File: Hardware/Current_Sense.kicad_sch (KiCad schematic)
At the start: 30 parts, among them IC1 INA241A5IDR, IC2 AMC1350DWVR, IC3 OPA396DCKR, J6 Shunt Resistor, J7 Scrut Conn, SW3 Scrut Select, U9 TLV6001DCK

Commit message: op amp
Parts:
- added IC4: TLV9002QDRQ1, SOIC127P600X175-8N, symbol TLV9002QDRQ1:TLV9002QDRQ1
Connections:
- net +3.3V: now also IC4.8 (V+)
- net GND: now also IC4.4 (V-)
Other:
- note added: "TODO: add voltage reference (~ 1.25V)"
- note removed: "TODO: voltage reference (~ 1.25V)"

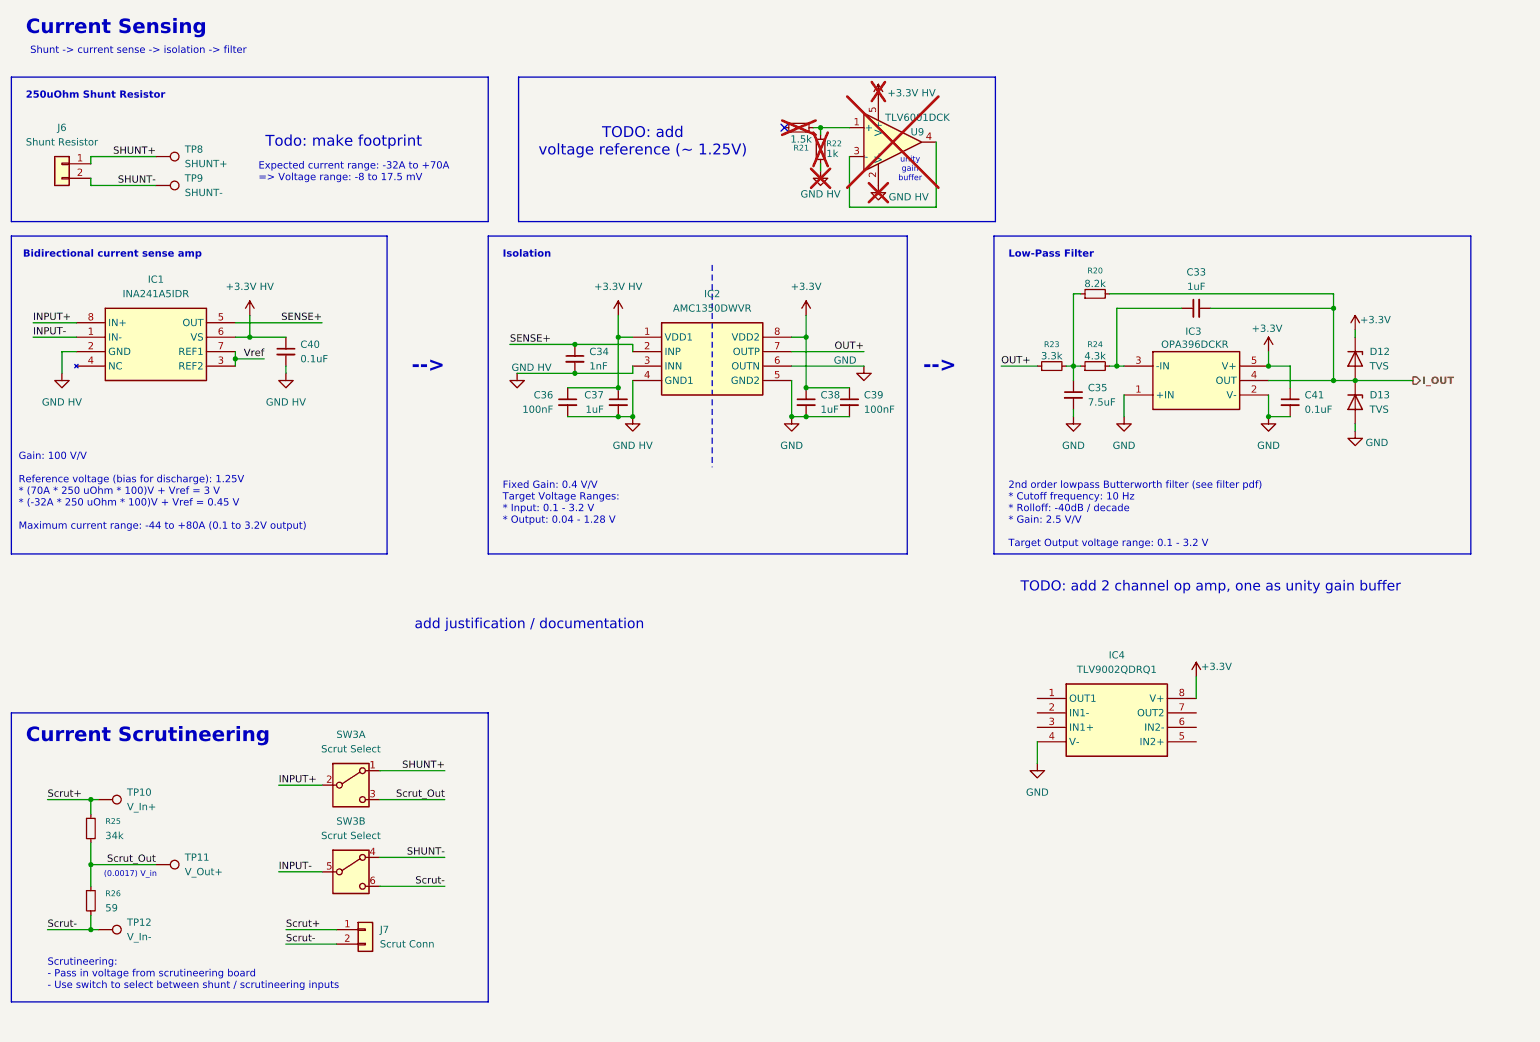
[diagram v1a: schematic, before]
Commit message: changed to 2 channel op amp, stole RPP from PSOM
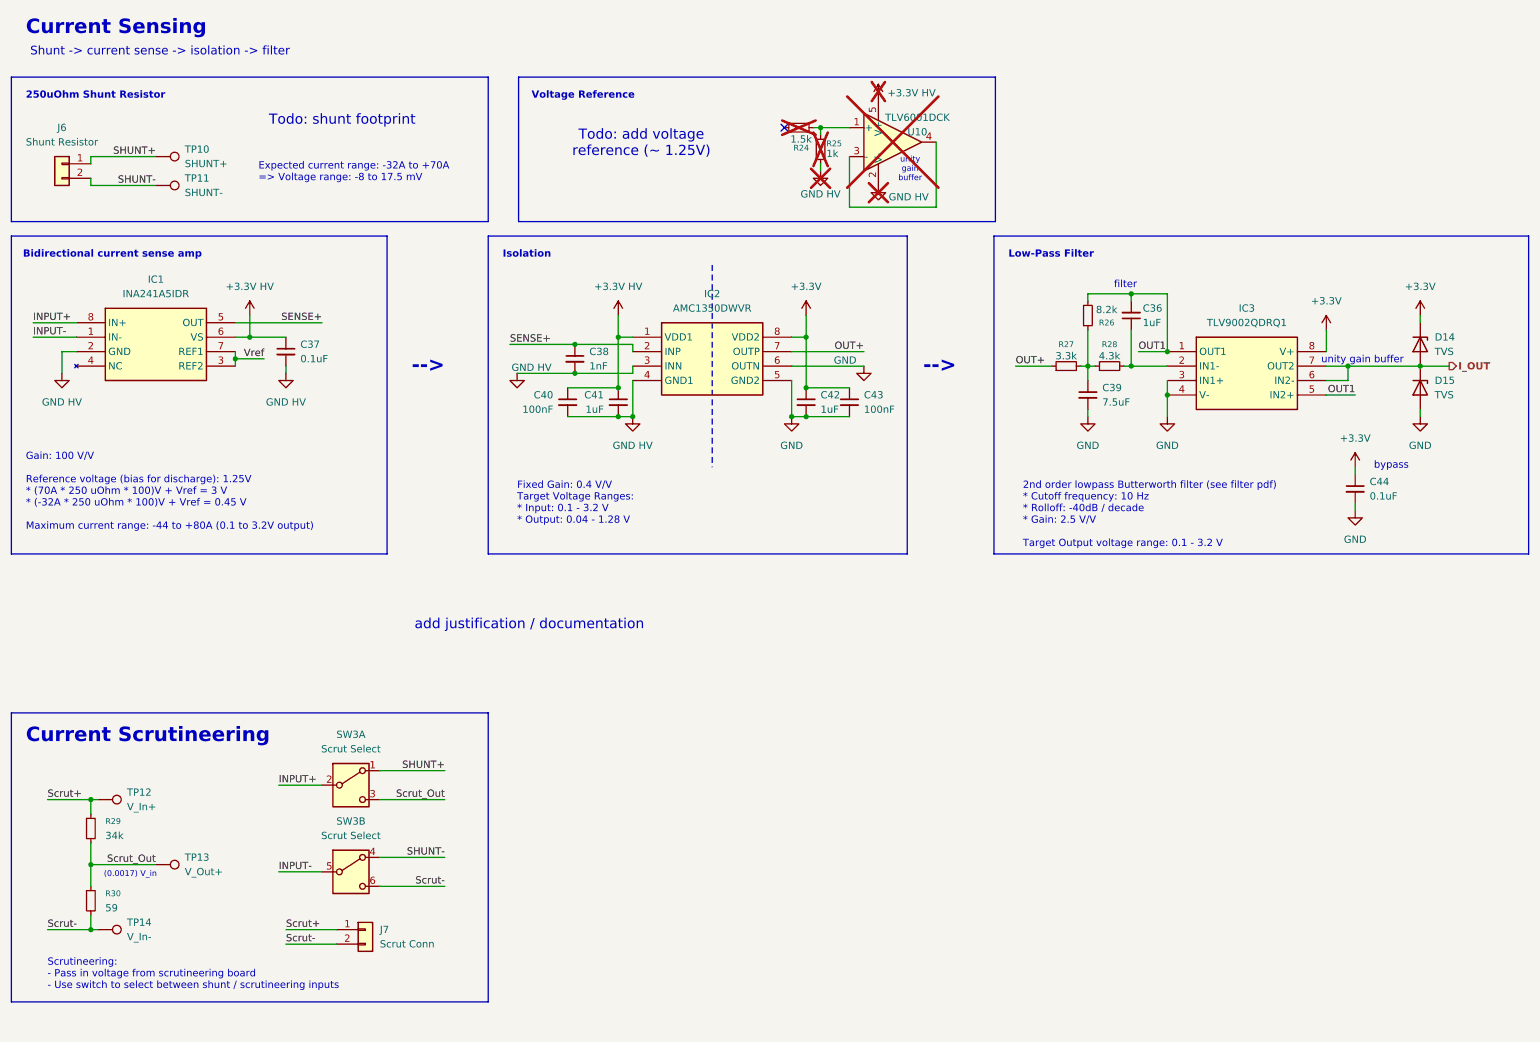
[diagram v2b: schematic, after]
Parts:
- removed C33: 1uF, Capacitor_SMD:C_0603_1608Metric_Pad1.08x0.95mm_HandSolder, symbol Device:C_Small
- removed C35: 7.5uF, Capacitor_SMD:C_0603_1608Metric_Pad1.08x0.95mm_HandSolder, symbol Device:C_Small
- removed C41: 0.1uF, Capacitor_SMD:C_0603_1608Metric_Pad1.08x0.95mm_HandSolder, symbol Device:C_Small
- removed D12, D13: TVS, Diode_SMD:D_SOD-123F, symbol Device:D_Zener
- removed IC3: OPA396DCKR, Parts:SOT65P210X110-5N, symbol OPA396DCKR:OPA396DCKR
- removed R20: 8.2k, Resistor_SMD:R_0603_1608Metric_Pad0.98x0.95mm_HandSolder, symbol Device:R_Small
- removed R23: 3.3k, Resistor_SMD:R_0603_1608Metric_Pad0.98x0.95mm_HandSolder, symbol Device:R_Small
- removed R24: 4.3k, Resistor_SMD:R_0603_1608Metric_Pad0.98x0.95mm_HandSolder, symbol Device:R_Small
- added C36: 1uF, Capacitor_SMD:C_0603_1608Metric_Pad1.08x0.95mm_HandSolder, symbol Device:C_Small
- added C39: 7.5uF, Capacitor_SMD:C_0603_1608Metric_Pad1.08x0.95mm_HandSolder, symbol Device:C_Small
- added C44: 0.1uF, Capacitor_SMD:C_0603_1608Metric_Pad1.08x0.95mm_HandSolder, symbol Device:C_Small
- added D14, D15: TVS, Diode_SMD:D_SOD-123F, symbol Device:D_Zener
- added R26: 8.2k, Resistor_SMD:R_0603_1608Metric_Pad0.98x0.95mm_HandSolder, symbol Device:R_Small
- added R27: 3.3k, Resistor_SMD:R_0603_1608Metric_Pad0.98x0.95mm_HandSolder, symbol Device:R_Small
- added R28: 4.3k, Resistor_SMD:R_0603_1608Metric_Pad0.98x0.95mm_HandSolder, symbol Device:R_Small
- renumbered C40 to C37, C34 to C38, C36 to C40, C37 to C41, C38 to C42, C39 to C43, IC4 to IC3, R21 to R24, R22 to R25, R25 to R29, R26 to R30, TP8 to TP10, TP9 to TP11, TP10 to TP12, TP11 to TP13, TP12 to TP14, U9 to U10
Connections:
- net +3.3V: now also C44.1, D14.1 (K)
- net GND: now also IC3.3 (IN1+), C39.2, C44.2, D15.2 (A)
- net I_OUT: now also IC3.6 (IN2-), IC3.7 (OUT2), D14.2 (A), D15.1 (K)
- net OUT+: now also R27.1
- net OUT1: now reaches IC3.1 (OUT1)
- net OUT1: now also IC3.5 (IN2+), C36.2, R26.2
- net at IC3.2 (IN1-): now also C36.1, R28.2
- new net: C39.1, R26.1, R27.2, R28.1
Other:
- note added: "Todo: add voltage reference (~ 1.25V)"
- note added: "Todo: shunt footprint"
- note added: "Voltage Reference"
- note added: "bypass"
- note added: "filter"
- note removed: "TODO: add 2 channel op amp, one as unity gain buffer"
- note removed: "TODO: add voltage reference (~ 1.25V)"
- note removed: "Todo: make footprint"
- moved on the sheet: IC3

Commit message: added voltage reference, shunt model; addressed comments
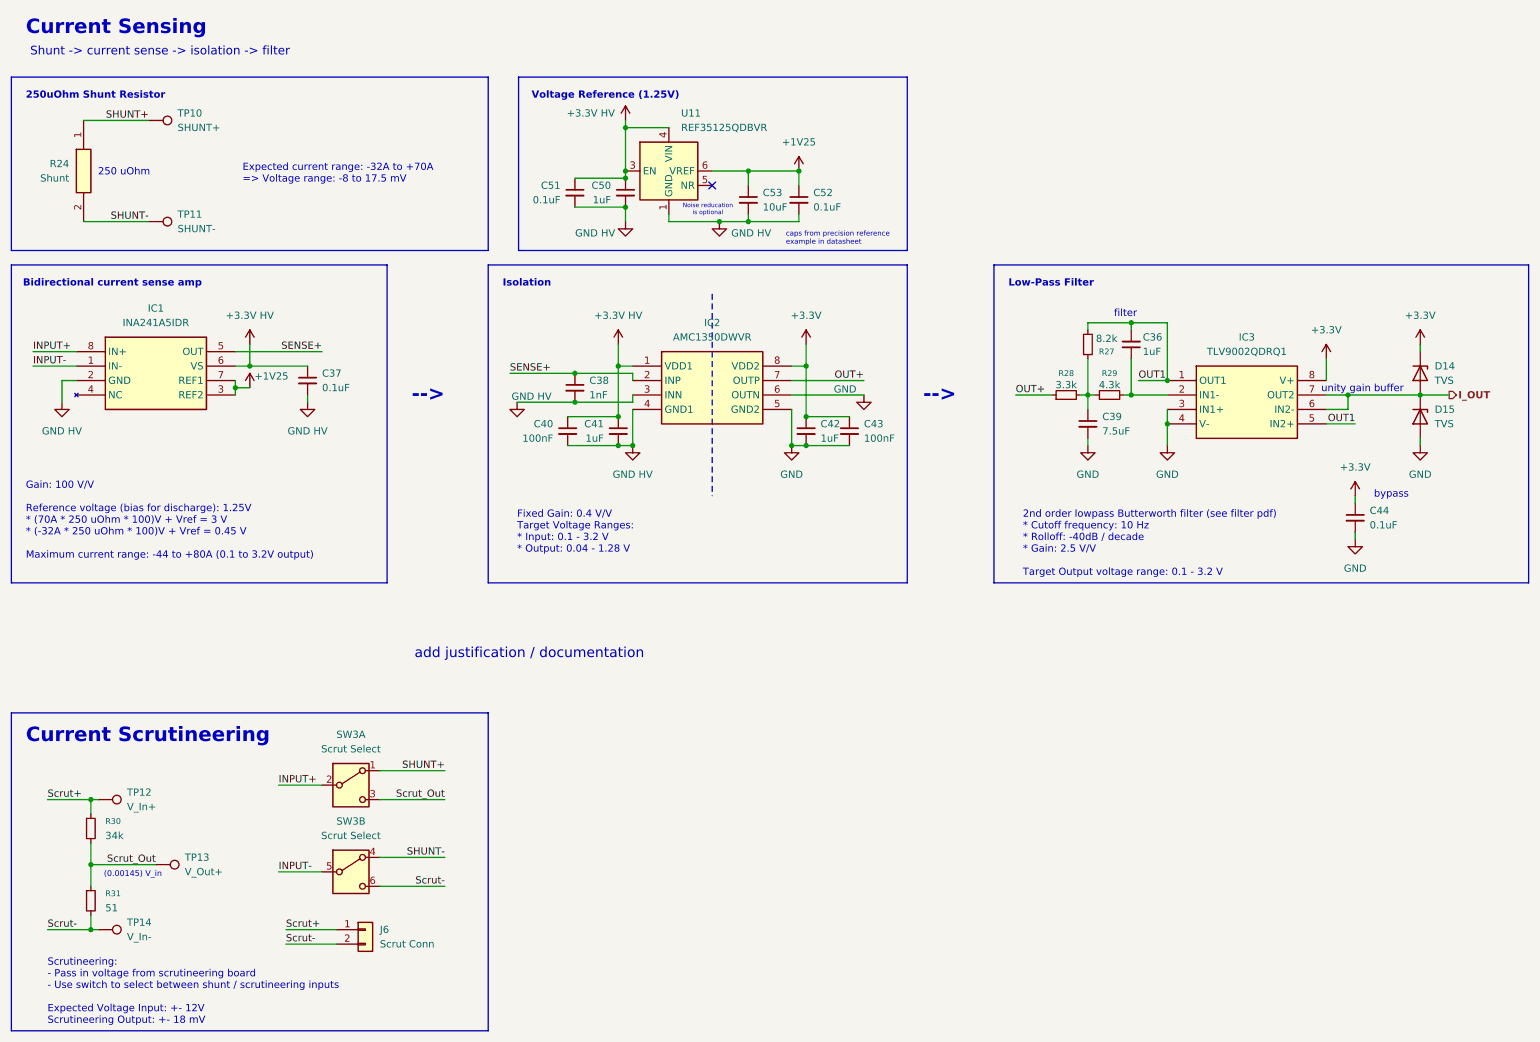
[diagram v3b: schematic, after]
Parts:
- removed J6: Shunt Resistor, symbol Connector_Generic:Conn_01x02
- removed R24: 1.5k, Resistor_SMD:R_0603_1608Metric_Pad0.98x0.95mm_HandSolder, symbol Device:R_Small
- removed R25: 1k, Resistor_SMD:R_0603_1608Metric_Pad0.98x0.95mm_HandSolder, symbol Device:R_Small
- removed U10: TLV6001DCK, Package_TO_SOT_SMD:SOT-353_SC-70-5, symbol Amplifier_Operational:TLV6001DCK
- added C50: 1uF, Capacitor_SMD:C_0603_1608Metric_Pad1.08x0.95mm_HandSolder, symbol Device:C_Small
- added C51, C52: 0.1uF, Capacitor_SMD:C_0603_1608Metric_Pad1.08x0.95mm_HandSolder, symbol Device:C_Small
- added C53: 10uF, Capacitor_SMD:C_0603_1608Metric_Pad1.08x0.95mm_HandSolder, symbol Device:C_Small
- added R24: Shunt, WSBS8518L2500JK, symbol WSBS8518L2500JK:WSBS8518L2500JK
- added U11: REF35125QDBVR, Package_TO_SOT_SMD:SOT-23-6, symbol Reference_Voltage:REF35125QDBVR
- R31: renamed from R30; value 59 -> 51
- renumbered J7 to J6, R26 to R27, R27 to R28, R28 to R29, R29 to R30
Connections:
- net +3.3V HV: now also C50.1, C51.1, U11.3 (EN), U11.4 (VIN)
- net GND HV: now also C50.2, C51.2, C52.2, C53.2, U11.1 (GND), U11.2 (GND)
- net SHUNT+: now also R24.1
- net SHUNT-: now also R24.2
- net Vref renamed +1V25
- net +1V25: now also C52.1, C53.1, U11.6 (VREF)
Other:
- note added: "(0.00145) V_in"
- note added: "250 uOhm"
- note added: "Noise reducation is optional"
- note added: "Scrutineering: - Pass in voltage from scrutineering board - Use switch to select between shunt / scrutineering inputs Expected Voltage Input: +- 12V Scrutineering Output: +- 18 mV"
- note added: "Voltage Reference (1.25V)"
- note added: "caps from precision reference example in datasheet"
- note removed: "(0.0017) V_in"
- note removed: "Scrutineering: - Pass in voltage from scrutineering board - Use switch to select between shunt / scrutineering inputs"
- note removed: "Todo: add voltage reference (~ 1.25V)"
- note removed: "Todo: shunt footprint"
- note removed: "Voltage Reference"
- moved on the sheet: C36, C37, C38, C39, C40, C41, C42, C43, C44, D14, D15, IC1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

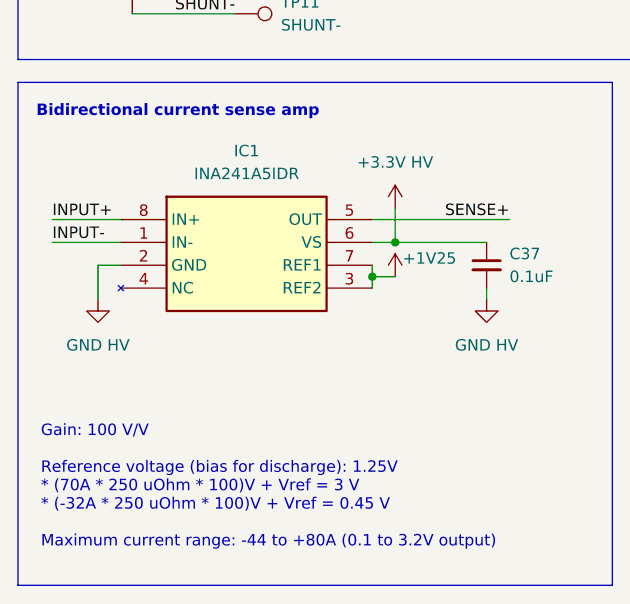
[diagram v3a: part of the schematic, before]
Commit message: cleaned up parts lib, correct INA ic listed
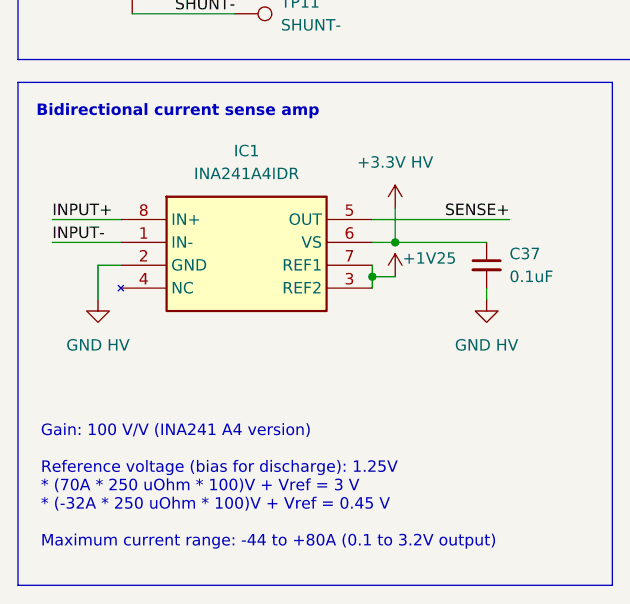
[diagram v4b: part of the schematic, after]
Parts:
- IC1: value INA241A5IDR -> INA241A4IDR; Manufacturer_Part_Number INA241A5IDR -> INA241A4IDR; Mouser Part Number 595-INA241A5IDR -> 595-INA241A4IDR; Mouser Price/Stock https://www.mouser.co.uk/ProductDetail/Texas-Instruments/IN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 -> https://www.mouser.com/ProductDetail/Texas-Instruments/INA2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
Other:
- note added: "Gain: 100 V/V (INA241 A4 version) Reference voltage (bias for discharge): 1.25V * (70A * 250 uOhm * 100)V + Vref = 3 V * (-32A * 250 uOhm * 100)V + Vref = 0.45 V Maximum current range: -44 to +80A (0.1 to 3.2V output)"
- note removed: "Gain: 100 V/V Reference voltage (bias for discharge): 1.25V * (70A * 250 uOhm * 100)V + Vref = 3 V * (-32A * 250 uOhm * 100)V + Vref = 0.45 V Maximum current range: -44 to +80A (0.1 to 3.2V output)"
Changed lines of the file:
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@@
 		)
 	)
-	(text "Gain: 100 V/V\n\nReference voltage (bias for discharge): 1.25V\n* (70A * 250 uOhm * 100)V + Vref = 3 V\n* (-32A * 250 uOhm * 100)V + Vref = 0.45 V\n\nMaximum current range: -44 to +80A (0.1 to 3.2V output)"
+	(text "Gain: 100 V/V (INA241 A4 version)\n\nReference voltage (bias for discharge): 1.25V\n* (70A * 250 uOhm * 100)V + Vref = 3 V\n* (-32A * 250 uOhm * 100)V + Vref = 0.45 V\n\nMaximum current range: -44 to +80A (0.1 to 3.2V output)"
 		(exclude_from_sim no)
 		(at 17.78 99.06 0)
@@
 	)
 	(image
-		(at 50.546 99.06)
-		(scale 0.288836)
+		(at 45.72 89.662)
+		(scale 0.258337)
 		(data "iVBORw0KGgoAAAANSUhEUgAAAbIAAAA4CAIAAAAXTepBAAAAA3NCSVQICAjb4U/gAAAACXBIWXMA"
 			"AA50AAAOdAFrJLPWAAAU5UlEQVR4nO2deSCU+R/Hv88zMwxmzCC5IiFX5B7JlWS7rNCh0pZuHSpb"
@@
 			)
 		)
-		(property "Value" "INA241A5IDR"
+		(property "Value" "INA241A4IDR"
 			(at 40.64 71.12 0)
 			(effects
@@
 			)
 		)
-		(property "Mouser Part Number" "595-INA241A5IDR"
+		(property "Mouser Part Number" "595-INA241A4IDR"
 			(at 50.8 571.12 0)
 			(effects
@@
 			)
 		)
-		(property "Mouser Price/Stock" "https://www.mouser.co.uk/ProductDetail/Texas-Instruments/INA241A5IDR?qs=ST9lo4GX8V3geNjZJSmQBQ%3D%3D"
+		(property "Mouser Price/Stock" "https://www.mouser.com/ProductDetail/Texas-Instruments/INA241A4IDR?qs=ST9lo4GX8V17OOIOvleTcQ%3D%3D"
 			(at 50.8 671.12 0)
 			(effects
@@
 			)
 		)
-		(property "Manufacturer_Part_Number" "INA241A5IDR"
+		(property "Manufacturer_Part_Number" "INA241A4IDR"
 			(at 50.8 871.12 0)
 			(effects
